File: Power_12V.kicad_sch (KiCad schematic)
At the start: 41 parts, among them J15 Conn_02x04_Top_Bottom, Q10 CSD18532Q5B, Q11 CSD18563Q5A, Q12 CSD18532Q5B, Q14 2N7002W, U13 LM5117PMH/NOPB

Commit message: pcb: added fans and thermistor to standard pcb
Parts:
- U13: LCSC (none) -> C390088; Part_Number (none) -> LM5117PMHX/NOPB
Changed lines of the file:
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@@
+			)
+		)
+		(property "Part_Number" "LM5117PMHX/NOPB"
+			(at 87.63 69.85 0)
+			(effects
+				(font
+					(size 1.27 1.27)
+				)
+				(hide yes)
+			)
+		)
+		(property "LCSC" "C390088"
+			(at 87.63 69.85 0)
+			(effects
+				(font
+					(size 1.27 1.27)
+				)
+				(hide yes)
 			)
 		)

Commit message: pcb: changed 1206 capacitors to 1210 since they are easier to source
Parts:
- C120, C76, C77, C78: footprint Capacitor_SMD:C_1206_3216Metric_Pad1.33x1.80mm_HandSolder -> Capacitor_SMD:C_1210_3225Metric_Pad1.33x2.70mm_HandSolder
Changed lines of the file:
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@@
 			)
 		)
-		(property "Footprint" "Capacitor_SMD:C_1206_3216Metric_Pad1.33x1.80mm_HandSolder"
+		(property "Footprint" "Capacitor_SMD:C_1210_3225Metric_Pad1.33x2.70mm_HandSolder"
 			(at 192.7352 78.74 0)
 			(effects
@@
 			)
 		)
-		(property "Footprint" "Capacitor_SMD:C_1206_3216Metric_Pad1.33x1.80mm_HandSolder"
+		(property "Footprint" "Capacitor_SMD:C_1210_3225Metric_Pad1.33x2.70mm_HandSolder"
 			(at 181.3052 78.74 0)
 			(effects
@@
 			)
 		)
-		(property "Footprint" "Capacitor_SMD:C_1206_3216Metric_Pad1.33x1.80mm_HandSolder"
+		(property "Footprint" "Capacitor_SMD:C_1210_3225Metric_Pad1.33x2.70mm_HandSolder"
 			(at 215.5952 78.74 0)
 			(effects
@@
 			)
 		)
-		(property "Footprint" "Capacitor_SMD:C_1206_3216Metric_Pad1.33x1.80mm_HandSolder"
+		(property "Footprint" "Capacitor_SMD:C_1210_3225Metric_Pad1.33x2.70mm_HandSolder"
 			(at 204.1652 78.74 0)
 			(effects

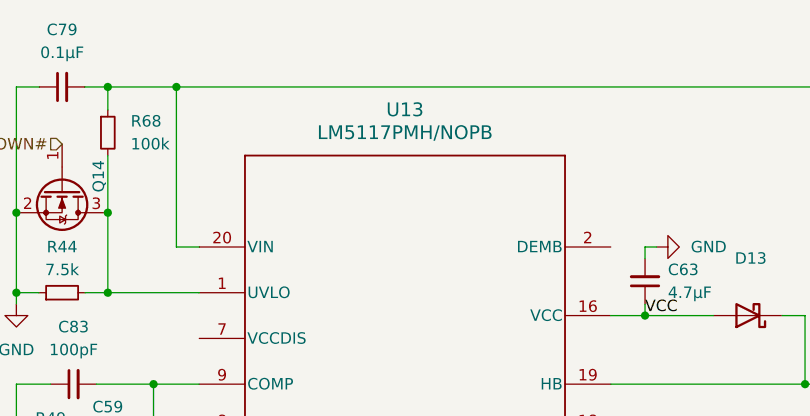
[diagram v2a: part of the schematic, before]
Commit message: pcb: reduced gate resistor in schematic review
Also updated some missing attributes.
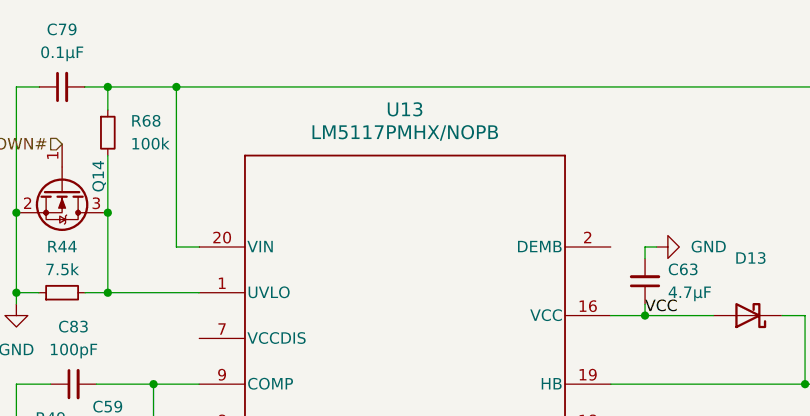
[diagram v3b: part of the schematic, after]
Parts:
- U13: value LM5117PMH/NOPB -> LM5117PMHX/NOPB
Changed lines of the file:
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@@
 			)
 		)
-		(property "Value" "LM5117PMH/NOPB"
+		(property "Value" "LM5117PMHX/NOPB"
 			(at 87.63 31.75 0)
 			(effects

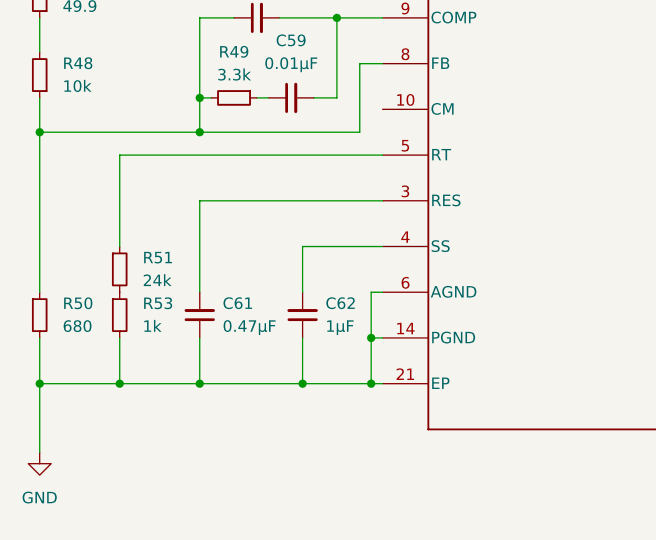
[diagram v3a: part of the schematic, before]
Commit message: pcb: disable hiccup mode on psu
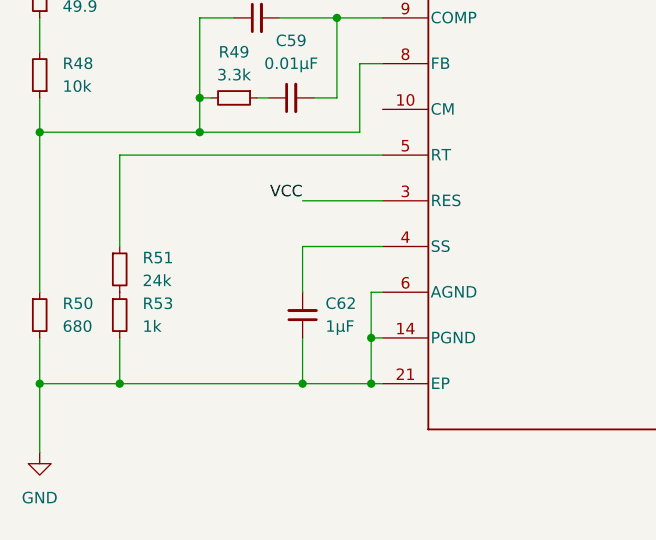
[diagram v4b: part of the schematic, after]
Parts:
- removed C61: 0.47µF, Capacitor_SMD:C_0402_1005Metric, symbol Device:C_Small
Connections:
- net VCC: now also U13.3 (RES)
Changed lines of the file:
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@@
 	)
 	(junction
-		(at 44.45 100.33)
-		(diameter 0)
-		(color 0 0 0 0)
-	)
-	(junction
 		(at 44.45 40.64)
 		(diameter 0)
@@
 	(wire
 		(pts
-			(xy 44.45 95.25) (xy 44.45 100.33)
-		)
-		(stroke
-			(width 0)
-			(type default)
-		)
-	)
-	(wire
-		(pts
 			(xy 62.23 26.67) (xy 151.13 26.67)
 		)
@@
 	(wire
 		(pts
-			(xy 44.45 80.01) (xy 44.45 90.17)
-		)
-		(stroke
-			(width 0)
-			(type default)
-		)
-	)
-	(wire
-		(pts
 			(xy 114.3 44.45) (xy 115.57 44.45)
 		)
@@
 	(wire
 		(pts
+			(xy 55.88 80.01) (xy 64.77 80.01)
+		)
+		(stroke
+			(width 0)
+			(type default)
+		)
+	)
+	(wire
+		(pts
 			(xy 63.5 100.33) (xy 64.77 100.33)
 		)
@@
 	(wire
 		(pts
-			(xy 44.45 100.33) (xy 35.56 100.33)
+			(xy 35.56 100.33) (xy 55.88 100.33)
 		)
 		(stroke
@@
 	(wire
 		(pts
-			(xy 64.77 80.01) (xy 44.45 80.01)
-		)
-		(stroke
-			(width 0)
-			(type default)
-		)
-	)
-	(wire
-		(pts
 			(xy 64.77 74.93) (xy 35.56 74.93)
 		)
@@
 	(wire
 		(pts
-			(xy 55.88 100.33) (xy 44.45 100.33)
-		)
-		(stroke
-			(width 0)
-			(type default)
-		)
-	)
-	(wire
-		(pts
 			(xy 26.67 53.34) (xy 26.67 54.61)
 		)
@@
 		)
 	)
+	(label "VCC"
+		(at 55.88 80.01 180)
+		(fields_autoplaced yes)
+		(effects
+			(font
+				(size 1.27 1.27)
+			)
+			(justify right bottom)
+		)
+	)
 	(hierarchical_label "SHUTDOWN#"
 		(shape input)
@@
 					(unit 1)
 				)
-			)
-		)
-	)
-	(symbol
-		(lib_id "Device:C_Small")
-		(at 44.45 92.71 180)
-		(unit 1)
-		(exclude_from_sim no)
-		(in_bom yes)
-		(on_board yes)
-		(dnp no)
-		(fields_autoplaced yes)
-		(property "Reference" "C61"
-			(at 46.99 91.4335 0)
-			(effects
-				(font
-					(size 1.27 1.27)
-				)
-				(justify right)
-			)
-		)
-		(property "Value" "0.47µF"
-			(at 46.99 93.9735 0)
-			(effects
-				(font
-					(size 1.27 1.27)
-				)
-				(justify right)
-			)
-		)
-		(property "Footprint" "Capacitor_SMD:C_0402_1005Metric"
-			(at 44.45 92.71 0)
-			(effects
-				(font
-					(size 1.27 1.27)
-				)
-				(hide yes)
-			)
-		)
-		(property "Datasheet" "~"
-			(at 44.45 92.71 0)
-			(effects
-				(font
-					(size 1.27 1.27)
-				)
-				(hide yes)
-			)
-		)
-		(property "Description" "Unpolarized capacitor, small symbol"
-			(at 44.45 92.71 0)
-			(effects
-				(font
-					(size 1.27 1.27)
-				)
-				(hide yes)
-			)
-		)
-		(property "Part_Number" "CL05A474KP5NNNC"
-			(at 44.45 92.71 90)
-			(effects
-				(font
-					(size 1.27 1.27)
-				)
-				(hide yes)
-			)
-		)
-		(property "LCSC" "C47339"
-			(at 44.45 92.71 90)
-			(effects
-				(font
-					(size 1.27 1.27)
-				)
-				(hide yes)
-			)
-		)
-		(pin "2"
-		)
-		(pin "1"
-		)
-		(instances
-			(project "XG_Mobile_Dock"
-				(path "/f97e6956-ab08-42cb-8fed-03fa58e87f0e/26322c8e-865a-4643-ac24-993508e41094"
-					(reference "C61")
-					(unit 1)
-				)
-				(path "/f97e6956-ab08-42cb-8fed-03fa58e87f0e/9c4a4d90-ef47-4134-81ea-2f9021c52e0b"
-					(reference "C81")
-					(unit 1)
-				)
